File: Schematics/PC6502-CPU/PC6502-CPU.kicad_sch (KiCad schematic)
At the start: 62 parts, among them J1 BUS, J4 TEST, J5 Conn_02x05_Odd_Even, J6 Conn_02x02_Odd_Even, U2 AS6C4008-55PCN, U3 SST39SF010, U4 ATF1502AS, U5 W65C02, U6 74AHC244, U8 MCP130-450DI/TO, X1 CXO_DIP8

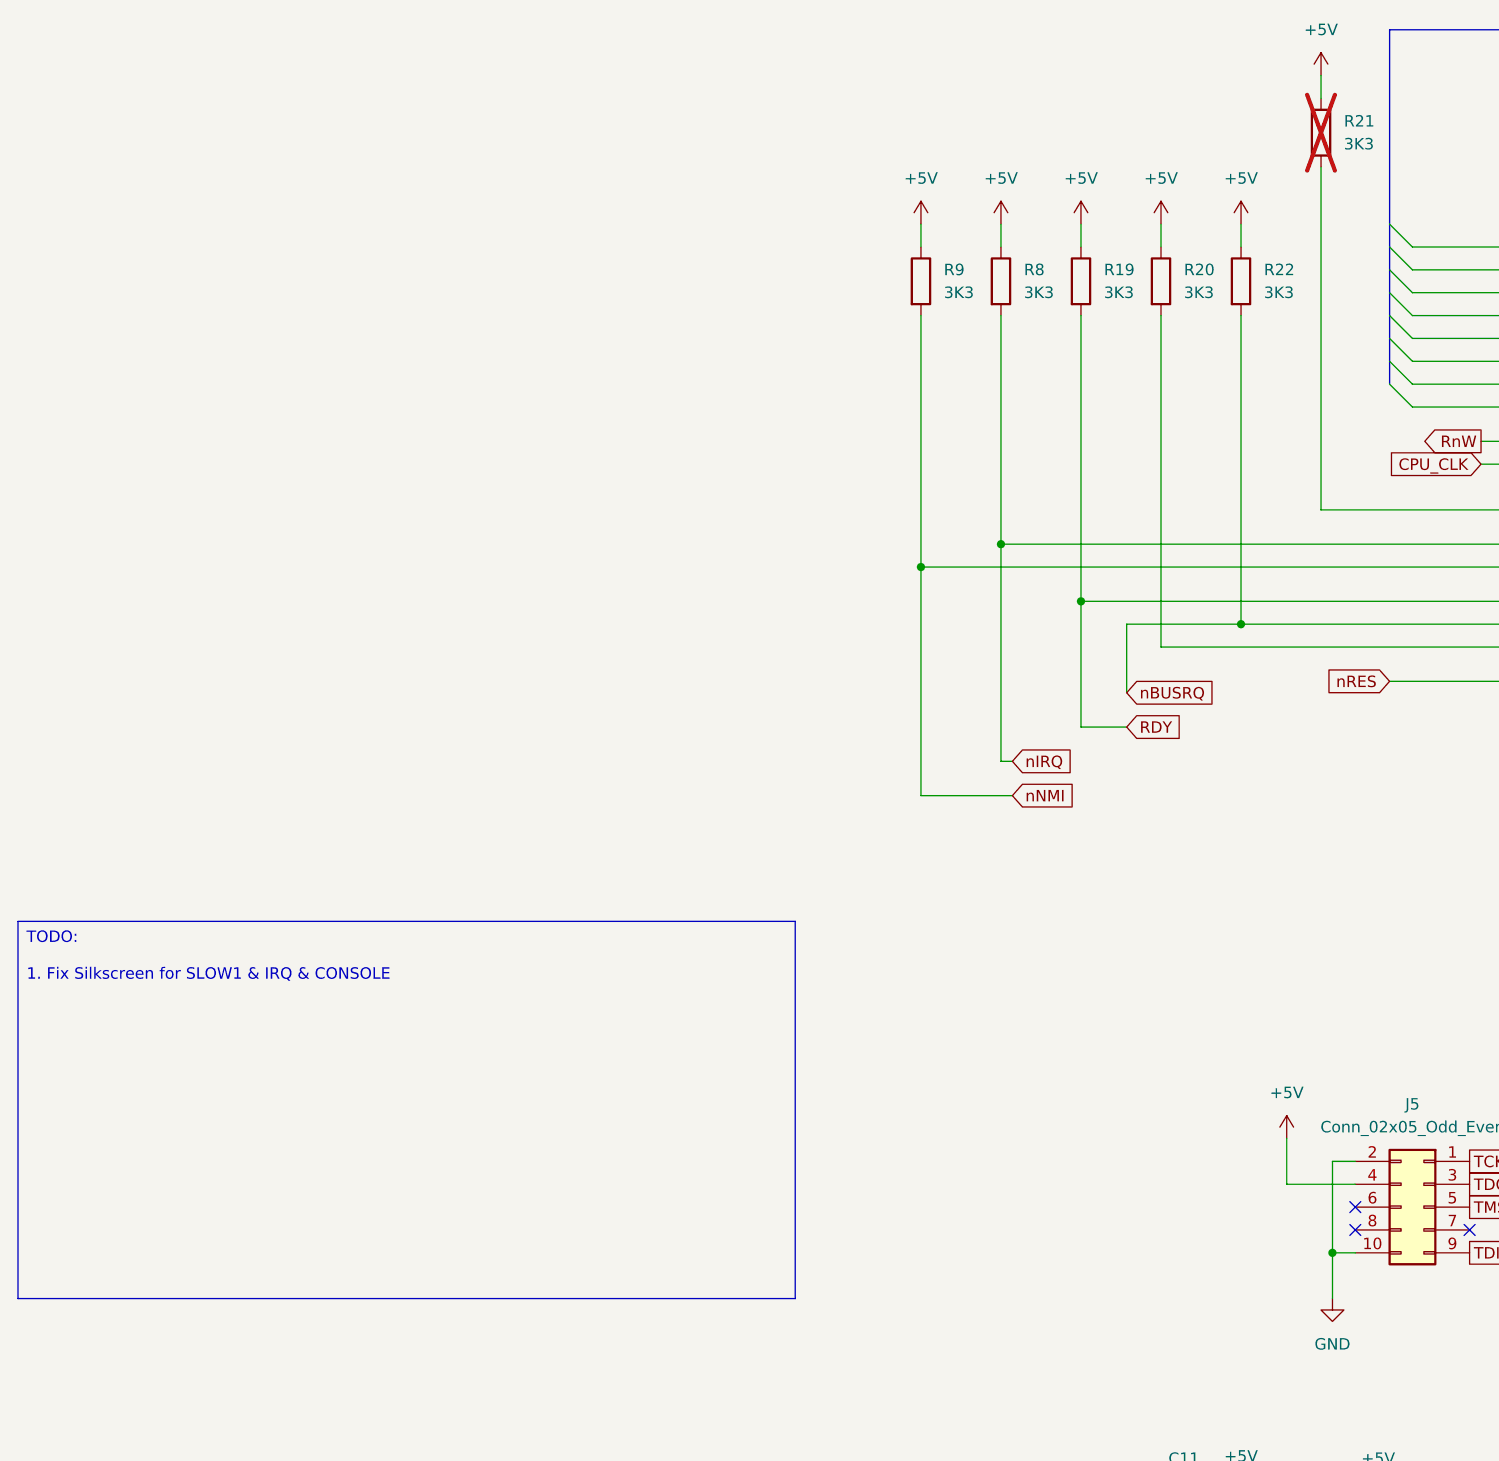
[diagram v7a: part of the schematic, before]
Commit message: Ordered Storage, FM/Speech, Dual SPI and APPLE II slot PCBs
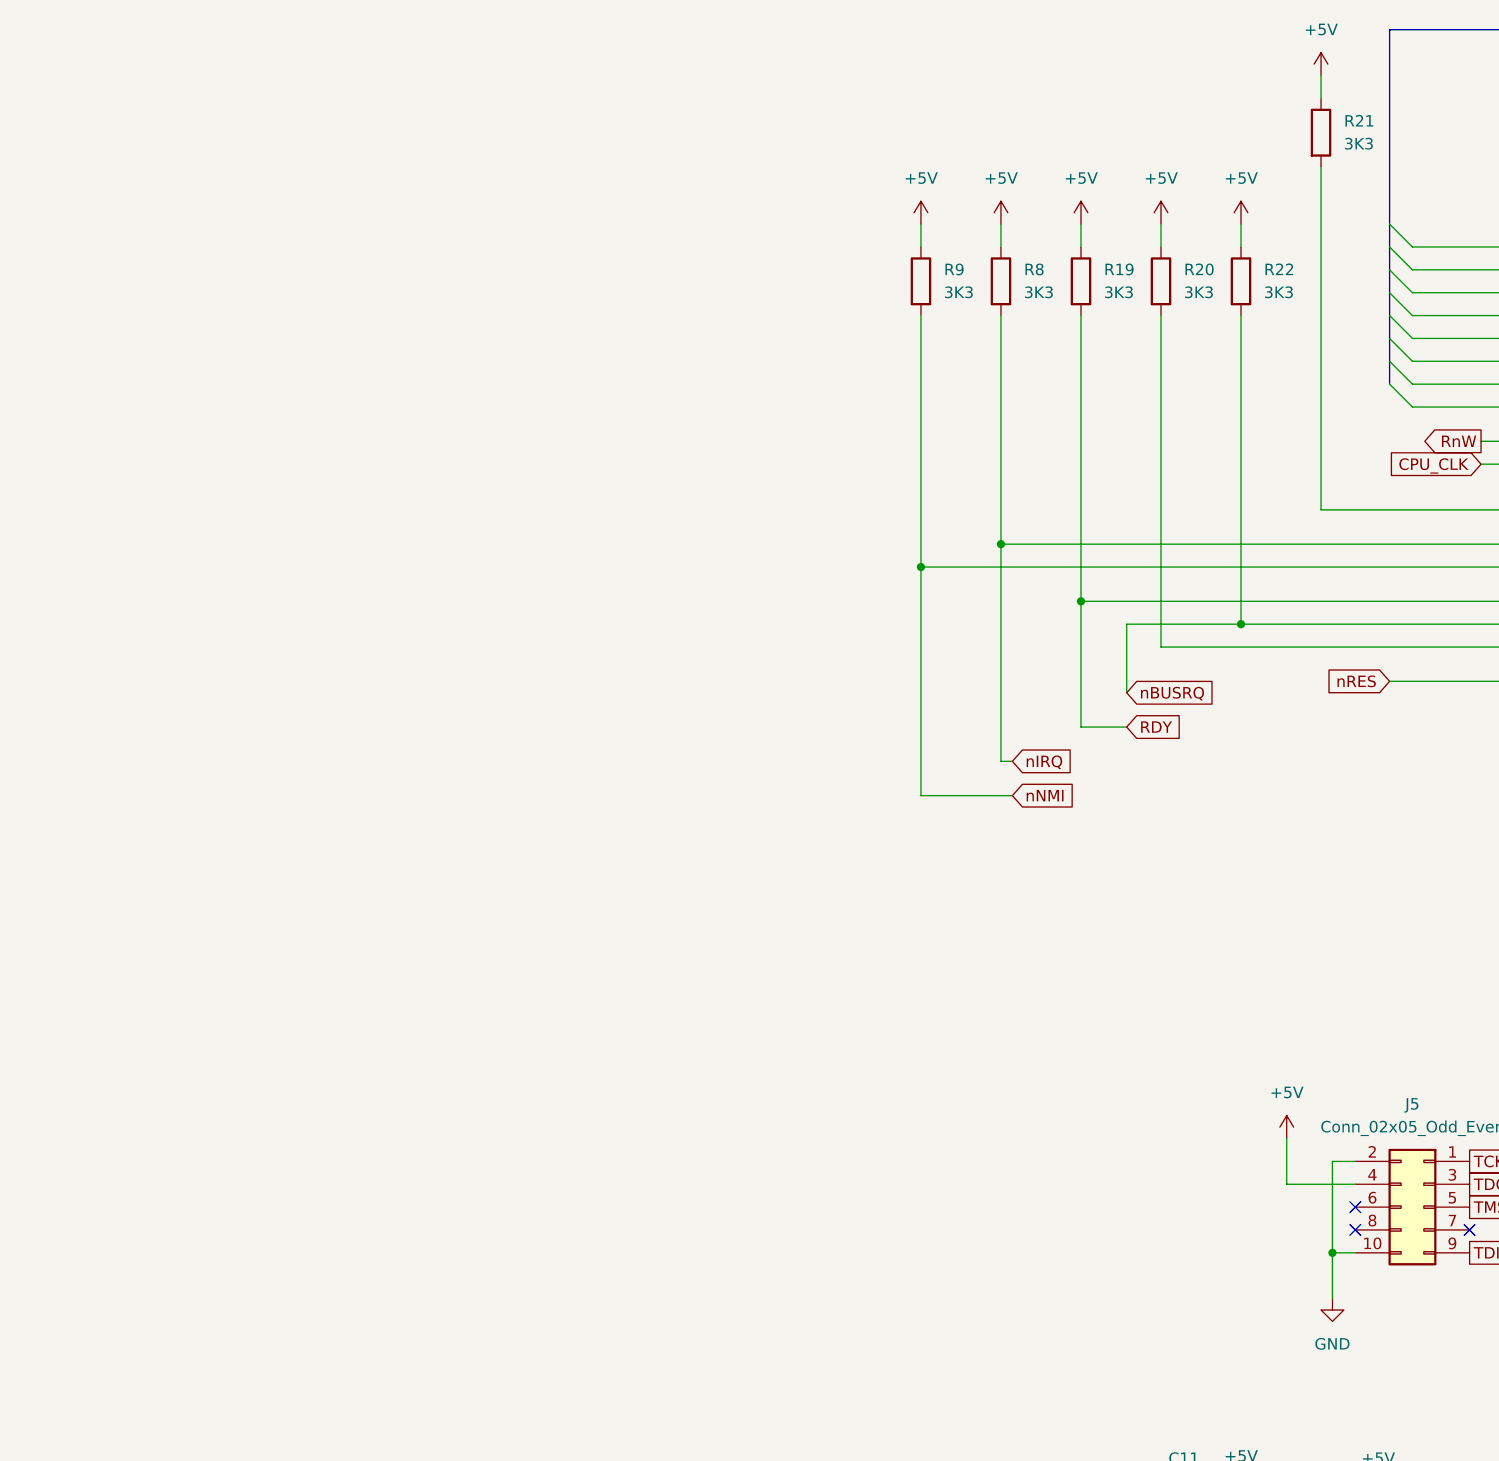
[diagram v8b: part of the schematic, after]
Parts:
- R21: now fitted
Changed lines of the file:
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@@
 		)
 	)
-	(text_box "TODO:\n\n1. Fix Silkscreen for SLOW1 & IRQ & CONSOLE\n"
-		(exclude_from_sim no)
-		(at -83.82 118.11 0)
-		(size 86.36 41.91)
-		(margins 0.9525 0.9525 0.9525 0.9525)
-		(stroke
-			(width 0)
-			(type solid)
-		)
-		(fill
-			(type none)
-		)
-		(effects
-			(font
-				(size 1.27 1.27)
-			)
-			(justify left top)
-		)
-	)
 	(junction
 		(at 189.23 229.87)
@@
 		(in_bom yes)
 		(on_board yes)
-		(dnp yes)
+		(dnp no)
 		(fields_autoplaced yes)
 		(property "Reference" "R21"
